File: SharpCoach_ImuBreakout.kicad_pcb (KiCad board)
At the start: 2 copper layers, 10 parts, among them J1 INTERFACE, U1 LIS3DH, U2 BMG250

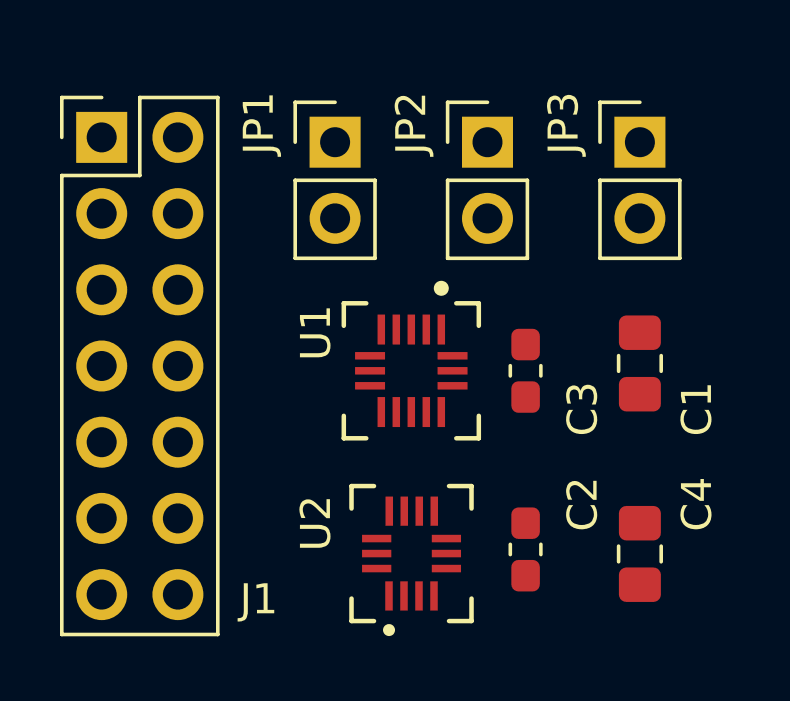
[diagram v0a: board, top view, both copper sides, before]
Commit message: Started PCB trace routing
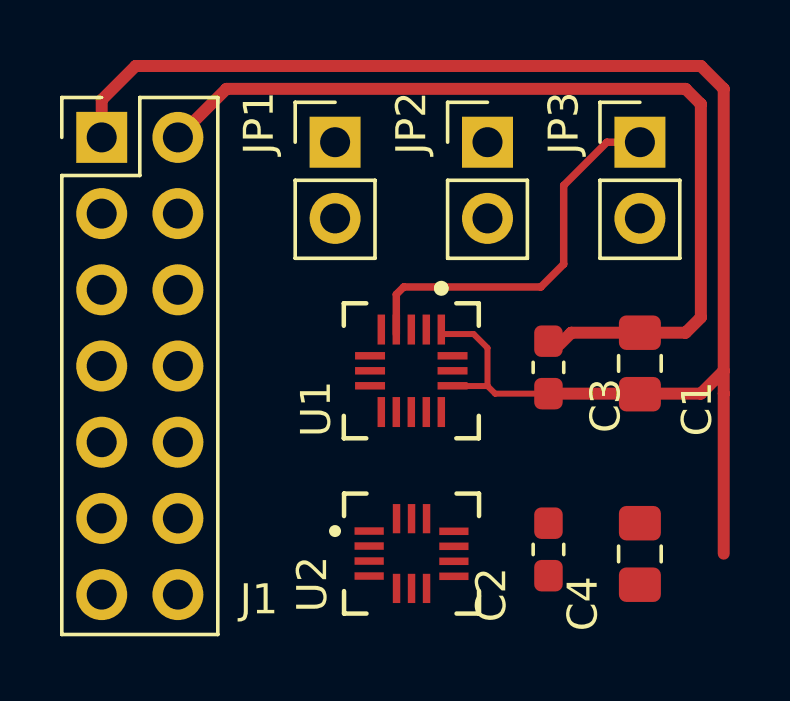
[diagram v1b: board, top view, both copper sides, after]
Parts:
- moved C3 0.77 mm to (151.9, 100.2)
- moved C2 0.76 mm to (151.9, 106.3), turned to 270 degrees
- turned C4 to 270 degrees
- turned U2 to 0 degrees
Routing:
- net +3V3: track 0.00 -> 50.8 mm
- net GND: track 0.00 -> 30.5 mm
- net /CLK_ACCEL: track 0.00 -> 13.1 mm
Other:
- net class Power added: clearance 0.2, trace_width 0.4, via_dia 0.8, via_drill 0.4

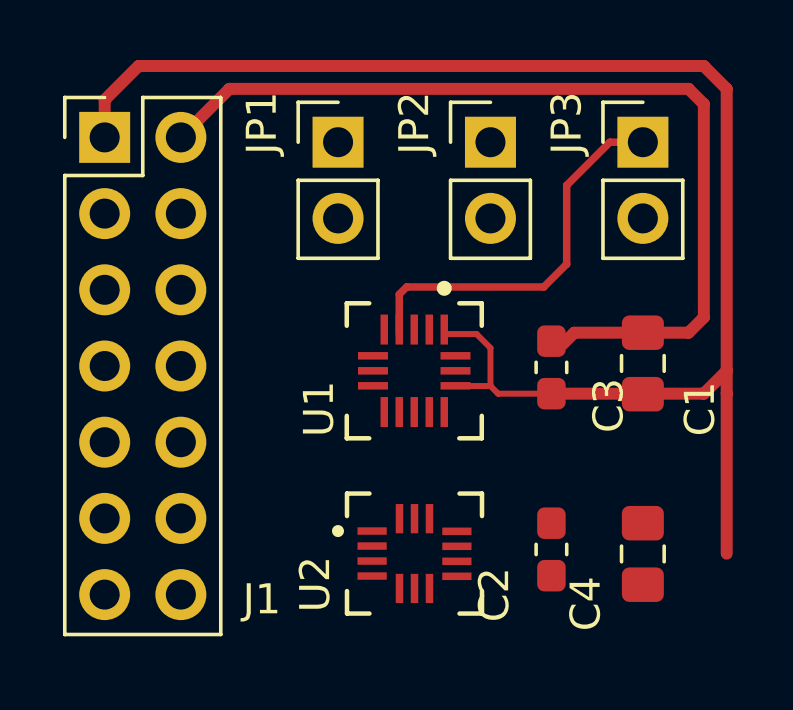
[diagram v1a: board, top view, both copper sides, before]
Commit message: Finished PCB trace routing.
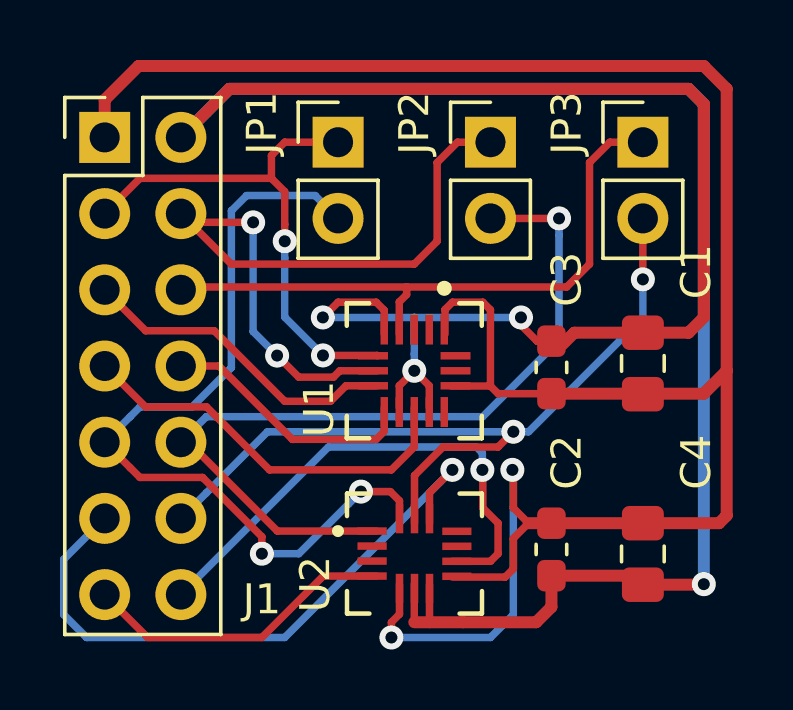
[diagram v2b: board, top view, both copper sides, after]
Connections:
- U1 pad 12: (no net) -> GND
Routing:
- net GND: track 30.5 -> 94.4 mm, vias 0 -> 4
- net /MISO_GYRO: track 0.00 -> 28.1 mm, vias 0 -> 1
- net /MOSI_GYRO: track 0.00 -> 28.0 mm, vias 0 -> 2
- net /CLK_GYRO: track 0.00 -> 27.2 mm, vias 0 -> 2
- net /MISO_ACCEL: track 0.00 -> 25.3 mm, vias 0 -> 2
- net +3V3: track 50.8 -> 75.2 mm, vias 0 -> 2
- net /CS_GYRO: track 0.00 -> 21.5 mm, vias 0 -> 1
- net /MOSI_ACCEL: track 0.00 -> 17.6 mm, vias 0 -> 2
- net /INT2_GYRO: track 0.00 -> 17.1 mm, vias 0 -> 1
- net /INT1_ACCEL: track 0.00 -> 13.4 mm
- net /CS_ACCEL: track 0.00 -> 10.8 mm
- net /INT1_GYRO: track 0.00 -> 10.5 mm
- net /INT2_ACCEL: track 0.00 -> 8.70 mm
- net /CLK_ACCEL: track 13.1 -> 21.1 mm

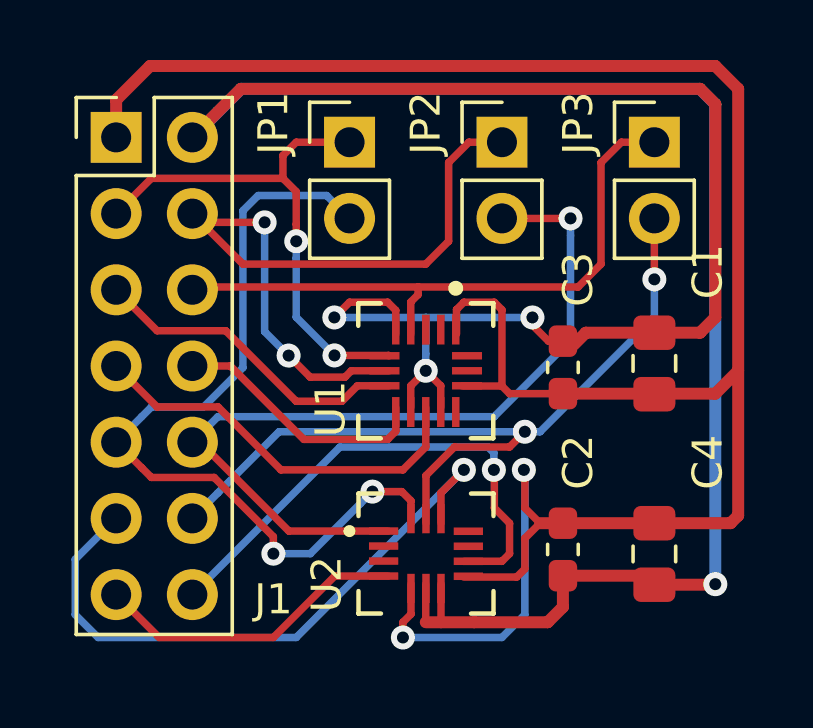
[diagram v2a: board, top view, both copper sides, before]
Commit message: Added copper pour and board outline to PCB layout.
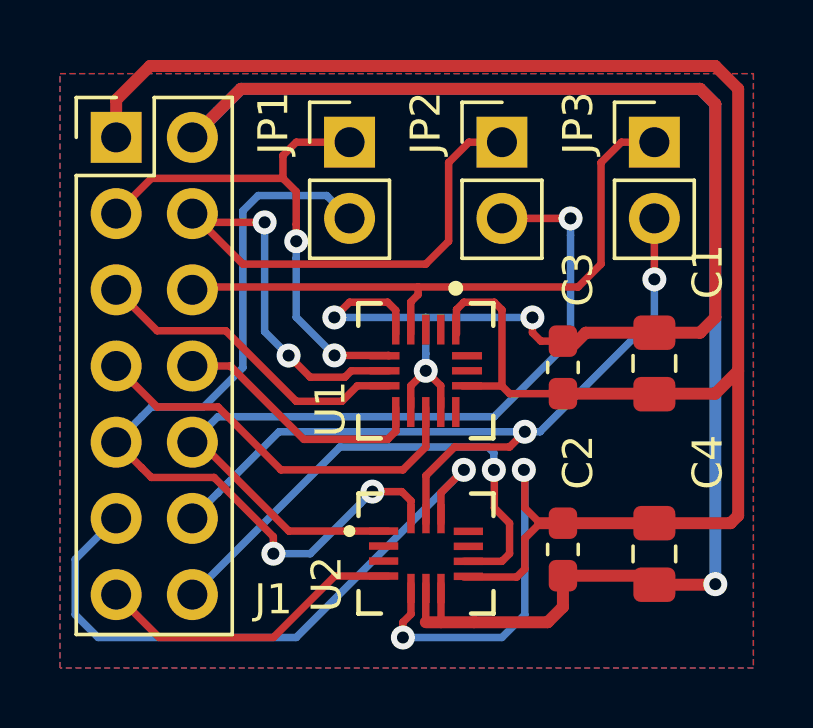
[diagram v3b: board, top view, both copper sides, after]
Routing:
- added copper zone on B.Cu, net GND
- added copper zone on F.Cu, net GND
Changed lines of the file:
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@@
   (general
     (thickness 1.6)
-    (drawings 0)
-    (tracks 208)
+    (drawings 4)
+    (tracks 209)
     (zones 0)
     (modules 10)
@@
     (user_trace_width 0.5)
     (trace_clearance 0.2)
-    (zone_clearance 0.508)
-    (zone_45_only no)
+    (zone_clearance 0.254)
+    (zone_45_only yes)
     (trace_min 0.2)
     (segment_width 0.2)
@@
     (pad_to_mask_clearance 0.2)
     (aux_axis_origin 0 0)
+    (grid_origin 134.366 89.154)
     (visible_elements 7FFDFFFF)
     (pcbplotparams
@@
       (net 10 /MISO_GYRO))
   )
+  (gr_line (start 134.366 110.998) (end 134.366 89.154) (layer Margin) (width 0.2))
+  (gr_line (start 159.004 110.998) (end 134.366 110.998) (layer Margin) (width 0.2))
+  (gr_line (start 159.004 89.154) (end 159.004 110.998) (layer Margin) (width 0.2))
+  (gr_line (start 134.366 89.154) (end 159.004 89.154) (layer Margin) (width 0.2))
   (segment (start 148.553 100.838) (end 148.545 100.83) (width 0.2) (layer F.Cu) (net 1))
   (segment (start 149.86 100.838) (end 148.553 100.838) (width 0.25) (layer F.Cu) (net 1))
@@
   (via (at 150.876 98.552) (size 0.8) (drill 0.4) (layers F.Cu B.Cu) (net 2))
   (segment (start 147.32 98.552) (end 150.876 98.552) (width 0.25) (layer B.Cu) (net 2))
-  (segment (start 151.412 99.342) (end 150.876 98.806) (width 0.25) (layer F.Cu) (net 2))
-  (segment (start 151.892 99.342) (end 151.412 99.342) (width 0.25) (layer F.Cu) (net 2))
   (segment (start 150.876 98.806) (end 150.876 98.552) (width 0.2) (layer F.Cu) (net 2))
+  (segment (start 150.876 99.06) (end 150.876 98.806) (width 0.25) (layer F.Cu) (net 2))
+  (segment (start 151.892 99.342) (end 151.158 99.342) (width 0.25) (layer F.Cu) (net 2))
+  (segment (start 151.158 99.342) (end 150.876 99.06) (width 0.25) (layer F.Cu) (net 2))
   (segment (start 137.000002 95.090002) (end 138.175003 93.915001) (width 0.25) (layer F.Cu) (net 3))
   (segment (start 138.175003 93.915001) (end 142.558999 93.915001) (width 0.25) (layer F.Cu) (net 3))
@@
   (segment (start 148.59 106.68) (end 149.86 106.68) (width 0.25) (layer F.Cu) (net 14))
   (segment (start 149.86 106.68) (end 150.114 106.426) (width 0.25) (layer F.Cu) (net 14))
+  (zone (net 2) (net_name GND) (layer F.Cu) (hatch edge 0.508)
+    (connect_pads (clearance 0.254))
+    (min_thickness 0.2)
+    (fill yes (arc_segments 16) (thermal_gap 0.508) (thermal_bridge_width 0.254))
+    (polygon
+      (pts
+        (xy 135.128 90.424) (xy 158.242 90.424) (xy 158.242 110.236) (xy 135.128 110.236)
+      )
+    )
+  )
+  (zone (net 2) (net_name GND) (layer B.Cu) (hatch edge 0.508)
+    (connect_pads (clearance 0.254))
+    (min_thickness 0.2)
+    (fill yes (arc_segments 16) (thermal_gap 0.508) (thermal_bridge_width 0.254))
+    (polygon
+      (pts
+        (xy 135.128 90.424) (xy 158.242 90.424) (xy 158.242 110.236) (xy 135.128 110.236)
+      )
+    )
+  )
+  (zone (net 0) (net_name "") (layer F.Cu) (hatch edge 0.508)
+    (connect_pads (clearance 0.254))
+    (min_thickness 0.2)
+    (keepout (tracks allowed) (vias allowed) (copperpour not_allowed))
+    (fill (arc_segments 16) (thermal_gap 0.8) (thermal_bridge_width 0.254))
+    (polygon
+      (pts
+        (xy 146.812 99.822) (xy 147.828 99.822) (xy 147.828 100.838) (xy 146.812 100.838)
+      )
+    )
+  )
 )

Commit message: Updated mask expansion to Oshpark recommended value of 2mil
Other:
- rule pad_to_mask_clearance: 0.2 -> 0.0508
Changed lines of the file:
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@@
     (pad_size 1.524 1.524)
     (pad_drill 0.762)
-    (pad_to_mask_clearance 0.2)
+    (pad_to_mask_clearance 0.0508)
     (aux_axis_origin 0 0)
     (grid_origin 134.366 89.154)

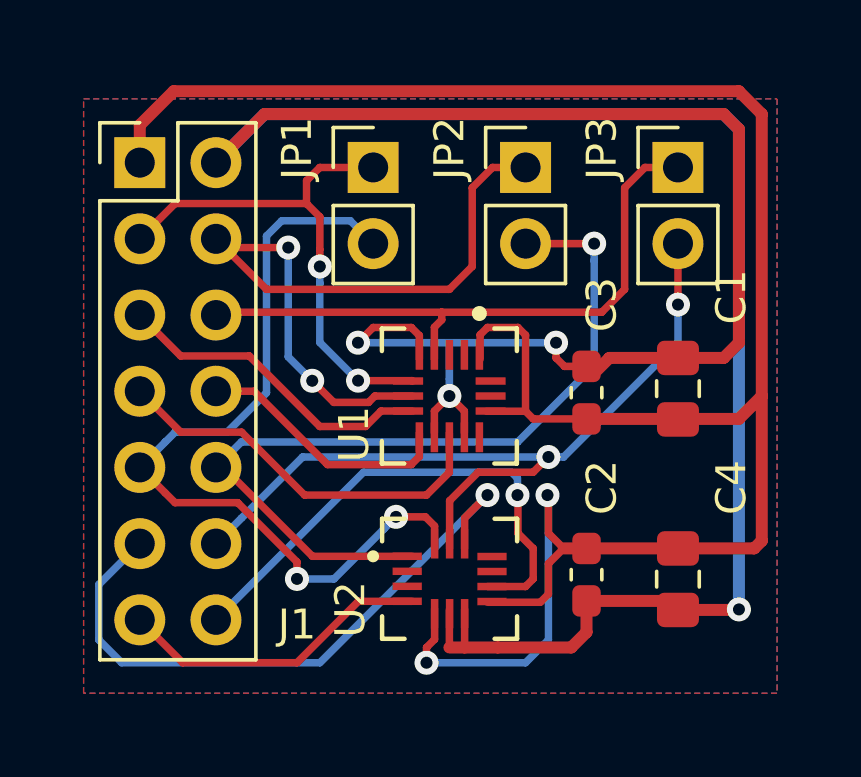
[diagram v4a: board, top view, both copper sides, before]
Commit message: Added title block info to schematic and board layout. Added design info to board silkscreen.
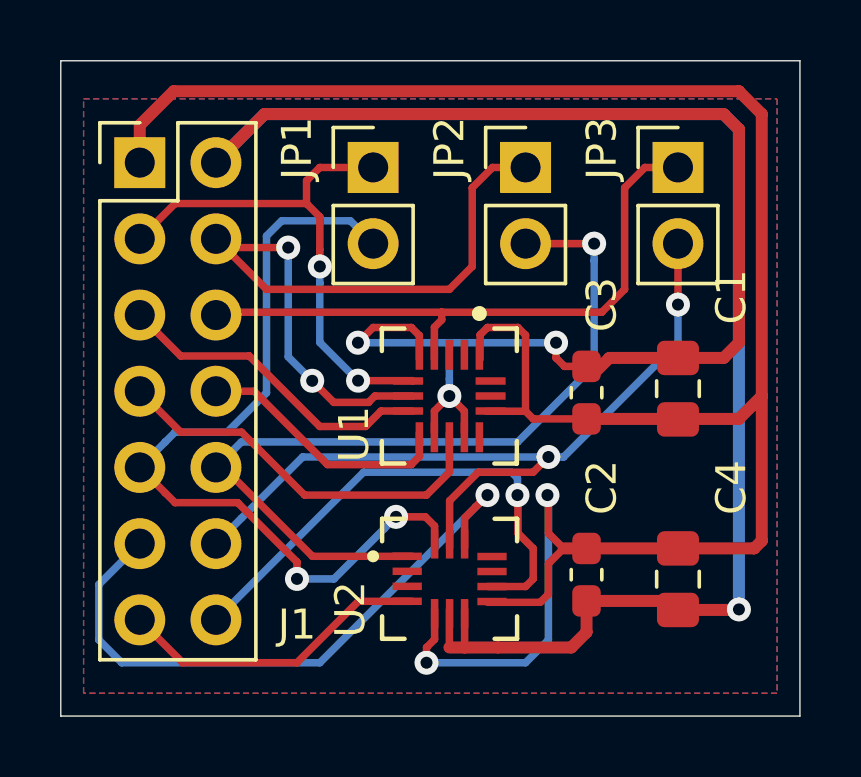
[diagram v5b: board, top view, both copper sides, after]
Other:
- board outline added: 24.6 x 21.8 mm
- board text added: "SharpCoach IMU Breakout v1 Kamil Rogozinski CC BY-SA 4.0"
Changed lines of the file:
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@@
   (general
     (thickness 1.6)
-    (drawings 4)
+    (drawings 9)
     (tracks 209)
     (zones 0)
@@
   )
   (page A4)
+  (title_block
+    (title "SharpCoach IMU Breakout")
+    (rev v1)
+    (company "Designed by: Kamil Rogozinski")
+    (comment 1 "License: CC BY-SA 4.0")
+  )
   (layers
     (0 F.Cu signal)
@@
     (43 Eco2.User user)
     (44 Edge.Cuts user)
-    (45 Margin user)
+    (45 Margin user hide)
     (46 B.CrtYd user)
     (47 F.CrtYd user)
@@
       (net 10 /MISO_GYRO))
   )
+  (gr_text "SharpCoach IMU Breakout v1\nKamil Rogozinski\nCC BY-SA 4.0" (at 158.242 92.202) (layer B.SilkS)
+    (effects (font (size 1 1) (thickness 0.15)) (justify left mirror))
+  )
+  (gr_line (start 134.366 110.998) (end 134.366 89.154) (layer Edge.Cuts) (width 0.05))
+  (gr_line (start 159.004 110.998) (end 134.366 110.998) (layer Edge.Cuts) (width 0.05))
+  (gr_line (start 159.004 89.154) (end 159.004 110.998) (layer Edge.Cuts) (width 0.05))
+  (gr_line (start 134.366 89.154) (end 159.004 89.154) (layer Edge.Cuts) (width 0.05))
   (gr_line (start 134.366 110.998) (end 134.366 89.154) (layer Margin) (width 0.2))
   (gr_line (start 159.004 110.998) (end 134.366 110.998) (layer Margin) (width 0.2))

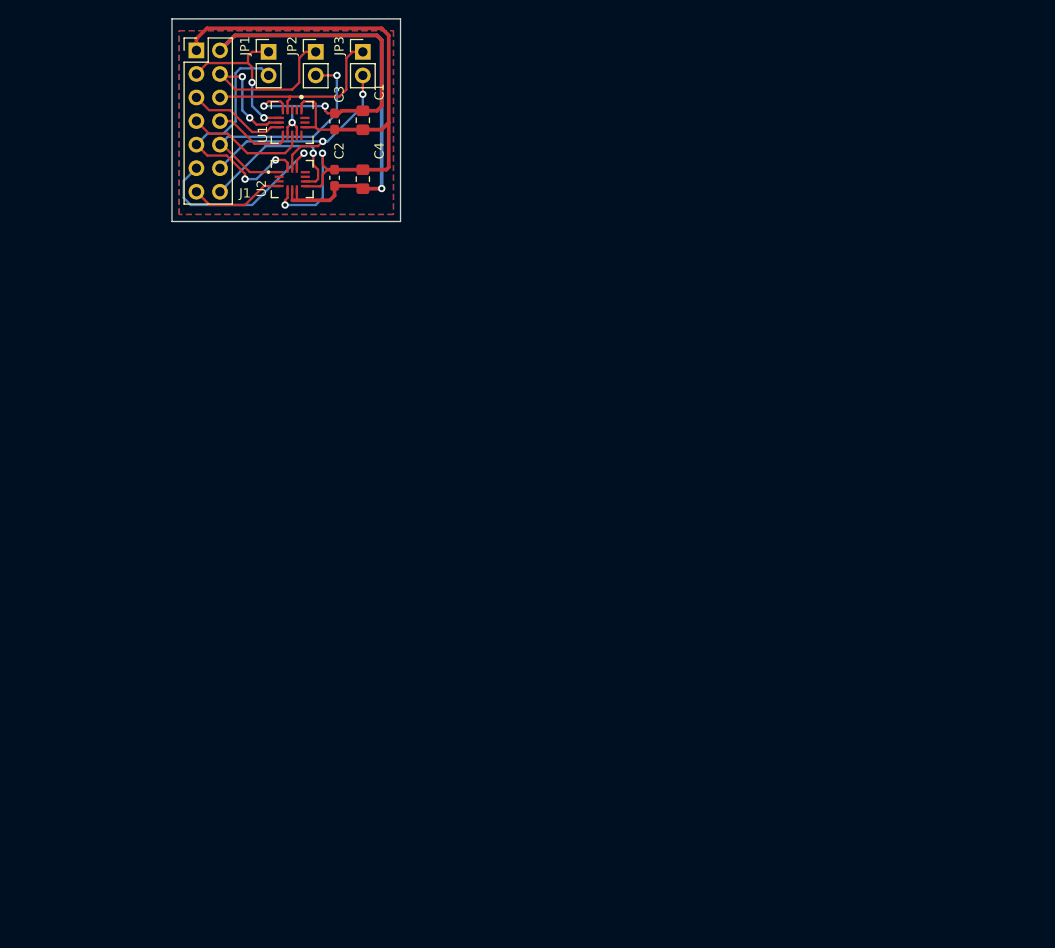
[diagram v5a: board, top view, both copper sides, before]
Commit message: Updated silkscreen layer for inertial sensor components.
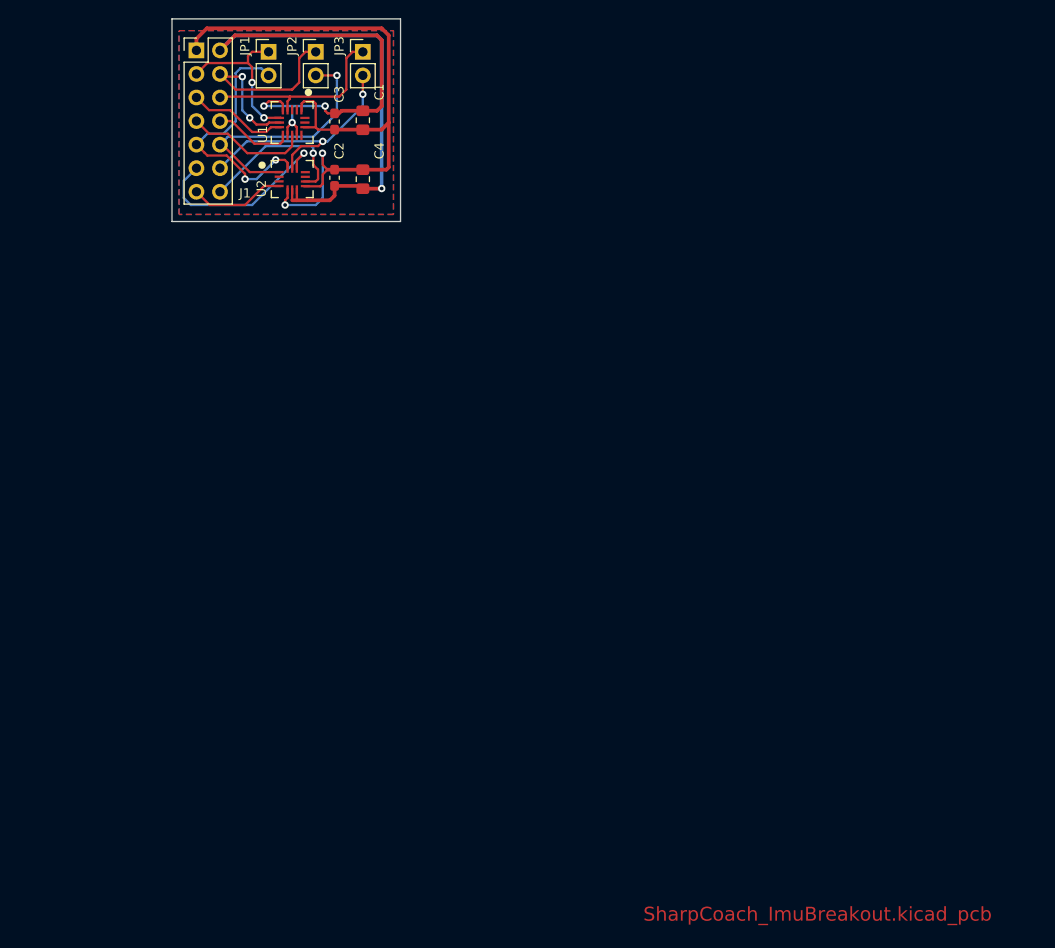
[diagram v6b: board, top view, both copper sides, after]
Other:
- board text added: "SharpCoach_ImuBreakout.kicad_pcb"
